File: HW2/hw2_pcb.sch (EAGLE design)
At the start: 0 parts

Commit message: Finished schematic
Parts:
- added C1, C2, C3, C4: 0.1uF, hw2_pcb:C-US025-025X050
- added C5, C6: 10uF, hw2_pcb:CPOL-USB45181B
- added J1: USB-MB-H, hw2_pcb:USB-MB-H
- added LED1: Red, hw2_pcb:LED3MM
- added LED2: Green, hw2_pcb:LED3MM
- added R1, R2: 330, hw2_pcb:R-US_0207/10
- added R3, R4: 10k, hw2_pcb:R-US_0207/10
- added U$1: PIC32MX250F128B, hw2_pcb:PIC32MX250F128B
- added U$10: PICKIT3, hw2_pcb:PICKIT3
- added U$2: SLIDE, hw2_pcb:SLIDE
- added U$3: MCP1702, hw2_pcb:MCP1702
- added U$4: RESET, hw2_pcb:PB
- added U$5: USER, hw2_pcb:PB
- added U$6, U$7: CONN_08, hw2_pcb:CONN_08
- added U$9: 8MHz, hw2_pcb:OSC
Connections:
- new net +3V3: C1.1, C2.1, C4.1, C6.+, LED1.A, R3.2, R4.2, U$1.13.VDD, U$1.23.VUSB3V3, U$1.28.AVDD, U$10.2.VDD, U$3.3.VOUT, U$7.2
- new net +5V: C3.1, U$1.15.VBUS, U$2.3, U$3.2.VIN, U$6.2
- new net A0: U$1.2.A0, U$7.8
- new net A1: U$1.3.A1, U$7.7
- new net A4/LED: LED2.A, U$1.12.A4/LED, U$7.3
- new net B13: U$1.24.B13, U$6.6
- new net B14: U$1.25.B14, U$6.7
- new net B15: U$1.26.B15, U$6.8
- new net B2: U$1.6.B2, U$7.6
- new net B3: U$1.7.B3, U$7.5
- new net B4/USER: R4.1, U$1.11.B4/USER, U$5.1, U$7.4
- new net B7: U$1.16.B7, U$6.3
- new net B8: U$1.17.B8, U$6.4
- new net B9: U$1.18.B9, U$6.5
- new net D+: J1.D+, U$1.21.D+/B10
- new net D-: J1.D-, U$1.22.D-/B11
- new net GND: C1.2, C2.2, C4.2, C5.-, C6.-, J1.GND, R1.1, R2.1, U$1.19.VSS, U$1.27.AVSS, U$1.8.VSS, U$10.3.VSS, U$3.1.GND, U$4.2, U$5.2, U$6.1, U$7.1, U$9.2.GND
- new net MCLR: R3.1, U$1.1.MCLR, U$10.1.MCLR, U$4.1
- new net N$1: J1.VBUS, U$2.2
- new net N$2: LED2.C, R2.2
- new net N$4: LED1.C, R1.2
- new net N$5: U$1.9.OSC1/A2, U$9.1.OSC1
- new net N$6: U$1.10.OSC2/A3, U$9.3.OSC2
- new net N$8: C5.+, U$1.20.VCAP
- new net PGC: U$1.5.PGEC1/B1, U$10.5.PCG
- new net PGD: U$1.4.PGED1/B0, U$10.4.PGD
- new net USBID: J1.ID, U$1.14.USBID/B5

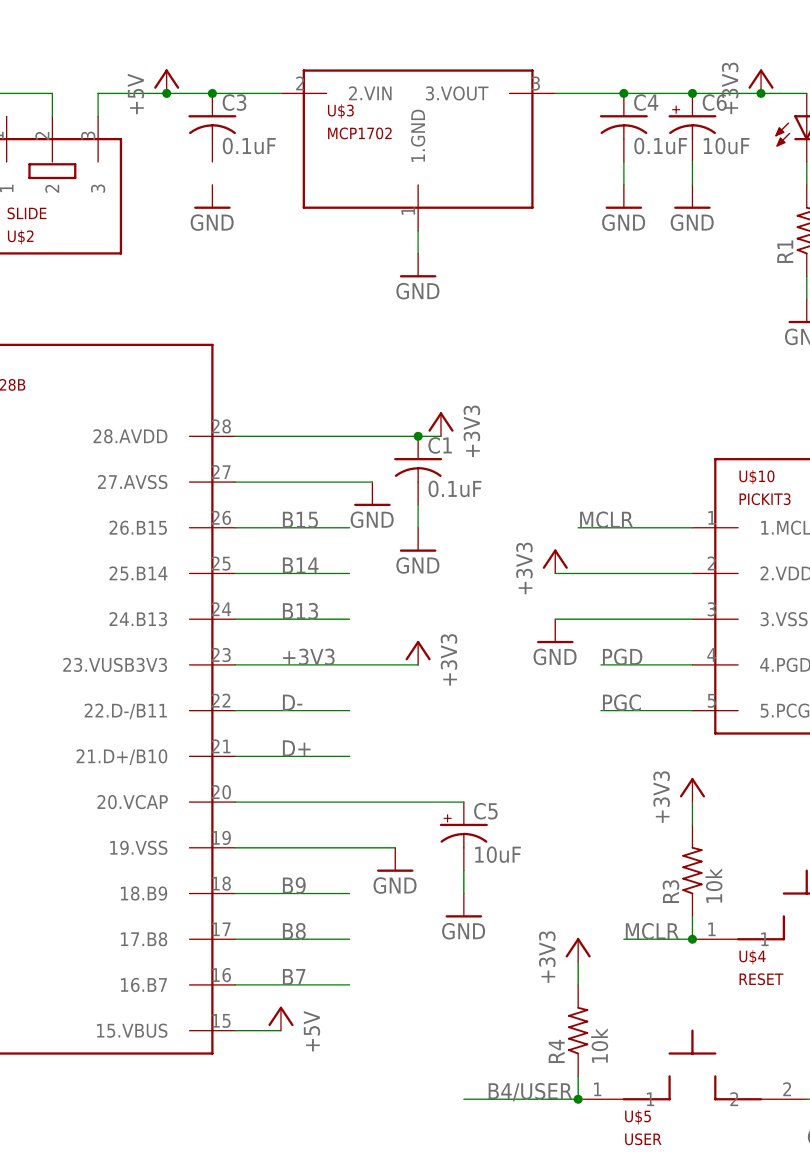
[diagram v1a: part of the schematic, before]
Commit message: Missed a ground connection on the schematic. Fixed it.
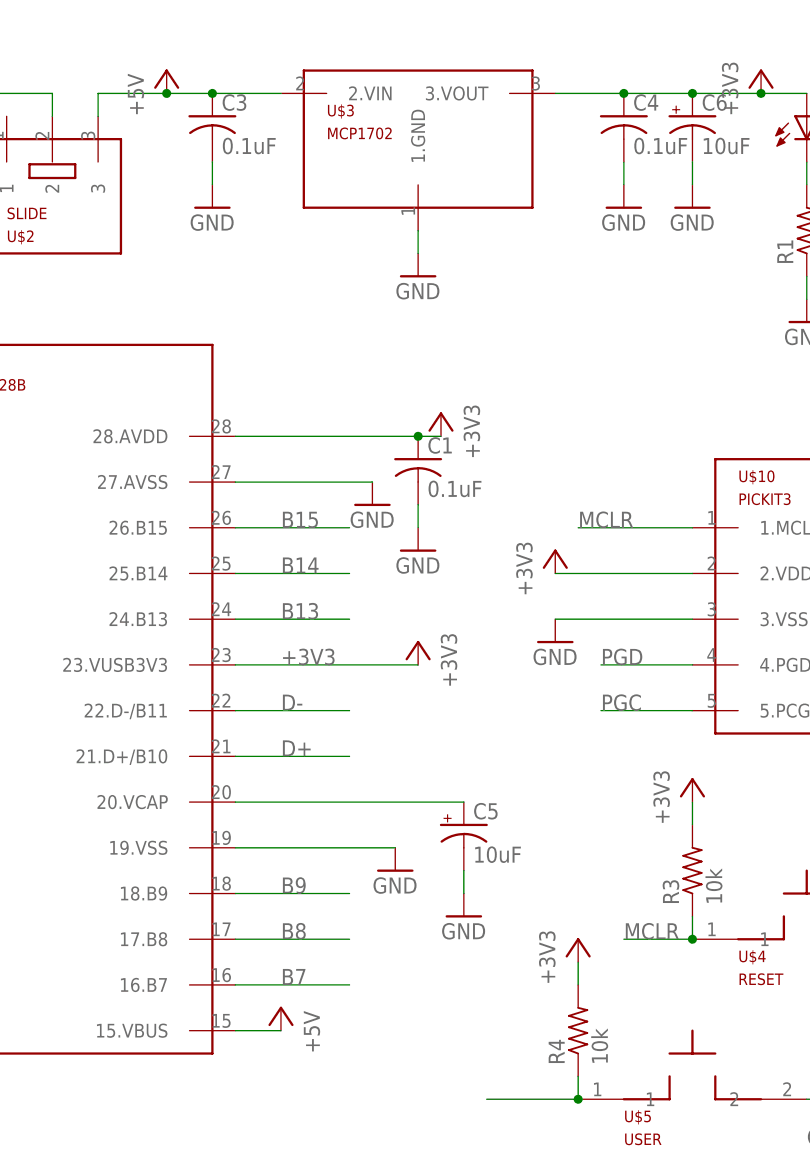
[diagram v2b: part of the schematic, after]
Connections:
- net GND: now also C3.2
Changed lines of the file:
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@@
 <wire x1="167.64" y1="-7.62" x2="172.72" y2="-7.62" width="0.1524" layer="91"/>
+</segment>
+<segment>
+<pinref part="C3" gate="G$1" pin="2"/>
+<pinref part="GND10" gate="1" pin="GND"/>
+<wire x1="68.58" y1="93.98" x2="68.58" y2="91.44" width="0.1524" layer="91"/>
 </segment>
 </net>
@@
 </segment>
 <segment>
-<pinref part="+3V5" gate="G$1" pin="+3V3"/>
-<pinref part="R4" gate="G$1" pin="2"/>
-<wire x1="109.22" y1="5.08" x2="109.22" y2="2.54" width="0.1524" layer="91"/>
-</segment>
-<segment>
 <pinref part="R3" gate="G$1" pin="2"/>
 <pinref part="+3V6" gate="G$1" pin="+3V3"/>
@@
 <pinref part="+3V7" gate="G$1" pin="+3V3"/>
 <wire x1="167.64" y1="-5.08" x2="190.5" y2="-5.08" width="0.1524" layer="91"/>
+</segment>
+<segment>
+<pinref part="R4" gate="G$1" pin="2"/>
+<pinref part="+3V5" gate="G$1" pin="+3V3"/>
+<wire x1="109.22" y1="2.54" x2="109.22" y2="5.08" width="0.1524" layer="91"/>
 </segment>
 </net>
@@
 </segment>
 <segment>
-<pinref part="R4" gate="G$1" pin="1"/>
-<pinref part="U$5" gate="G$1" pin="1"/>
-<wire x1="109.22" y1="-7.62" x2="109.22" y2="-10.16" width="0.1524" layer="91"/>
-<wire x1="109.22" y1="-10.16" x2="96.52" y2="-10.16" width="0.1524" layer="91"/>
-<junction x="109.22" y="-10.16"/>
-<label x="99.06" y="-10.16" size="1.778" layer="95"/>
-</segment>
-<segment>
 <pinref part="U$7" gate="G$1" pin="4"/>
 <wire x1="167.64" y1="0" x2="185.42" y2="0" width="0.1524" layer="91"/>
 <label x="172.72" y="0" size="1.778" layer="95"/>
 </segment>
-</net>
+<segment>
+<pinref part="U$5" gate="G$1" pin="1"/>
+<pinref part="R4" gate="G$1" pin="1"/>
+<wire x1="109.22" y1="-10.16" x2="109.22" y2="-7.62" width="0.1524" layer="91"/>
+<wire x1="109.22" y1="-10.16" x2="99.06" y2="-10.16" width="0.1524" layer="91"/>
+<junction x="109.22" y="-10.16"/>
+</segment>
+</net>
